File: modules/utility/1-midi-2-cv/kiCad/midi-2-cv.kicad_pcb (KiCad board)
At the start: 2 copper layers, 101 x 110 mm, 174 parts, among them J1 Conn_01x03, J3 SD-50BV (DIN5), J4 Conn_01x03, J5 BOOT_RUN, J6 Conn_01x04, Q1 BC848, Q2 BC848, Q3 BC848, Q4 BC848, SW1 ON-OFF-ON, U1 6N135, U10 MCP4728, U11 STM32F411RETx, U2 L78L05_SOT89, U3 MCP4728, U4 TL074, U5 MCP4728, U6 TL074, U7 AMS1117-3.3, U8 TL074, U9 TL074, Y2 20MHZ

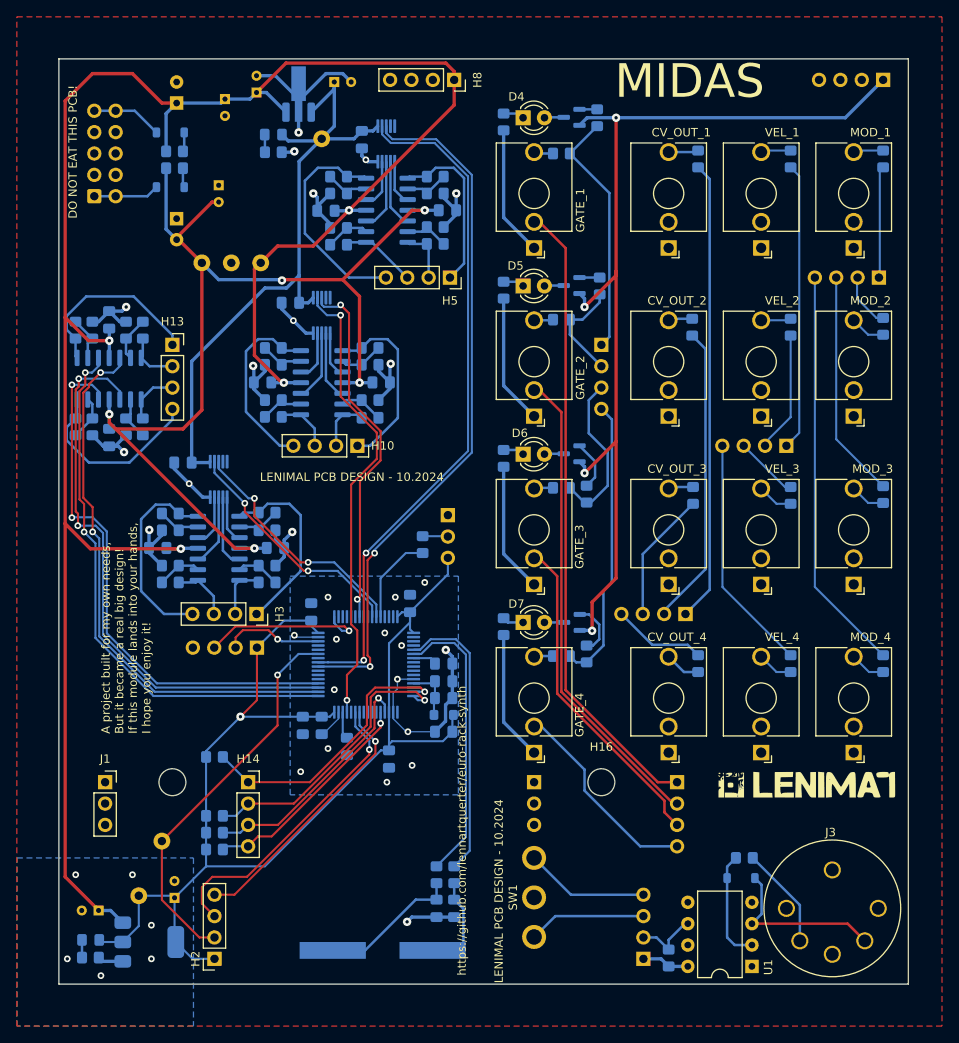
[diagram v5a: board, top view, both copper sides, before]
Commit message: debugging and rework for ricochet, midas, wolkje. Added IBOM for drums and other modules.
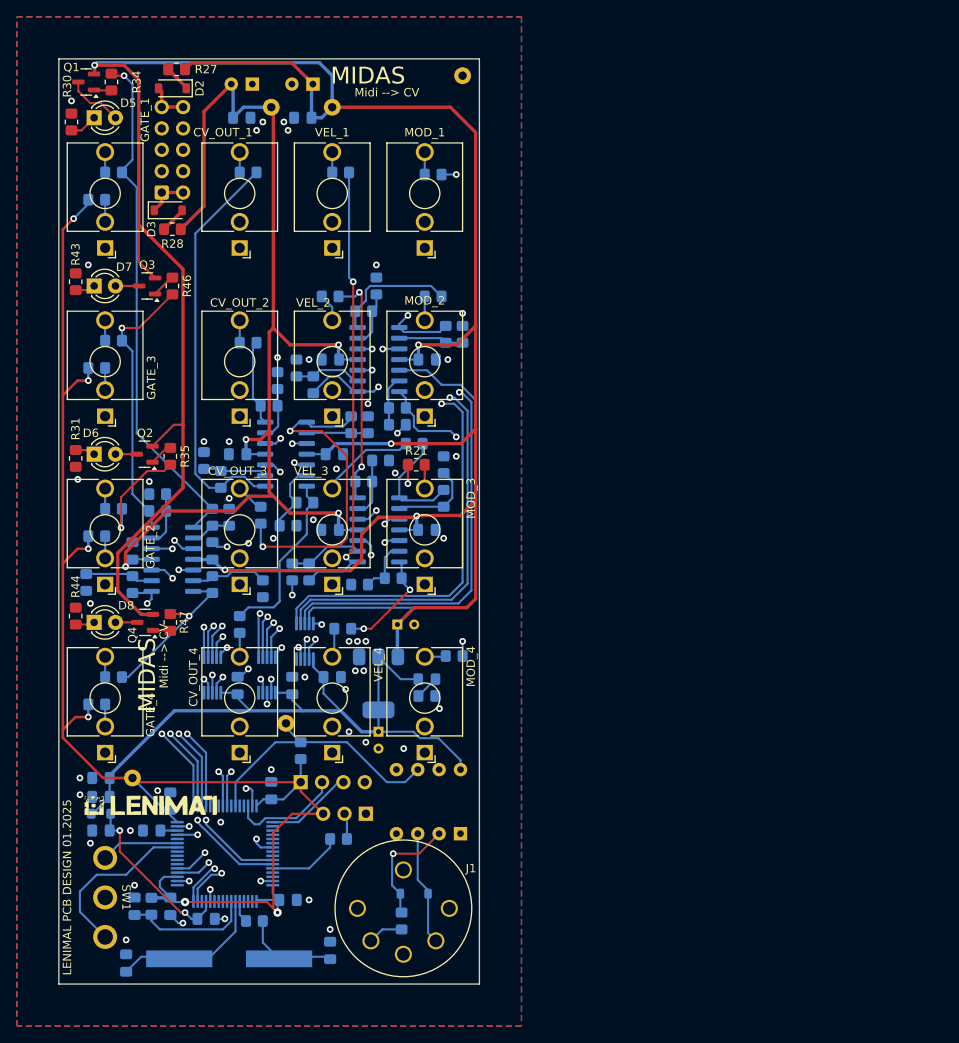
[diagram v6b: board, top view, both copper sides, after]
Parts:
- removed C30, C31, C32, C34: 100nF, Capacitor_SMD:C_0805_2012Metric_Pad1.18x1.45mm_HandSolder
- removed C33: 10uF, Capacitor_SMD:C_0805_2012Metric_Pad1.18x1.45mm_HandSolder
- removed C35: 10nF, Capacitor_SMD:C_0805_2012Metric_Pad1.18x1.45mm_HandSolder
- removed C36, C37: 1uF, Capacitor_SMD:C_0805_2012Metric_Pad1.18x1.45mm_HandSolder
- removed C38, C39: 10pF, Capacitor_SMD:C_0805_2012Metric_Pad1.18x1.45mm_HandSolder
- removed C40: 2.2uF, Capacitor_SMD:C_0805_2012Metric_Pad1.18x1.45mm_HandSolder
- removed the D8 at (75.5, 59.0)
- removed D9: LED, LED_SMD:LED_0805_2012Metric_Pad1.15x1.40mm_HandSolder
- removed the G*** at (139.0, 136.3)
- removed the G*** at (86.0, 139.5)
- removed the G*** at (139.1, 136.2)
- removed H10, H13, H14, H2, H3, H5, H8: PinSocket_01x04, Synth:PinSocket_1x04_P2.54mm_Vertical
- removed H11, H12, H15, H4, H6, H9: PinHeader_01x04, Synth:PinHeader_1x04_P2.54mm_Vertical
- removed H16, H17: MountingHole, MountingHole:MountingHole_3.2mm_M3
- removed H7: Conn_02x05_PWR_Eurorack, Synth:IDC-Header_2x05_P2.54mm_Vertical
- removed the J1 at (55.5, 136.0)
- removed J4: Conn_01x03, Connector_PinHeader_2.54mm:PinHeader_1x03_P2.54mm_Vertical
- removed J5: BOOT_RUN, Connector_PinHeader_2.54mm:PinHeader_1x03_P2.54mm_Vertical
- removed J6: Conn_01x04, Connector_PinHeader_2.54mm:PinHeader_1x04_P2.54mm_Vertical
- removed R70, R71: 2K, Resistor_SMD:R_0805_2012Metric_Pad1.20x1.40mm_HandSolder
- removed TP6: MIDI_IN, Connector_Pin:Pin_D1.0mm_L10.0mm
- removed U9: TL074, Synth:SOIC-14
- removed Y2: 20MHZ, Crystal:Crystal_SMD_HC49-SD_HandSoldering
- added C18: 100nF, Capacitor_SMD:C_0805_2012Metric_Pad1.18x1.45mm_HandSolder, B.Cu at (75.2, 137.0)
- added C19: 100nF, Capacitor_SMD:C_0805_2012Metric_Pad1.18x1.45mm_HandSolder, B.Cu at (63.2, 138.2)
- added C20: 100nF, Capacitor_SMD:C_0805_2012Metric_Pad1.18x1.45mm_HandSolder, B.Cu at (77.2, 150.0)
- added C21: 100nF, Capacitor_SMD:C_0805_2012Metric_Pad1.18x1.45mm_HandSolder, B.Cu at (63.2, 150.8)
- added C22: 10uF, Capacitor_SMD:C_0805_2012Metric_Pad1.18x1.45mm_HandSolder, B.Cu at (55.0, 135.5)
- added C23: 100nF, Capacitor_SMD:C_0805_2012Metric_Pad1.18x1.45mm_HandSolder, B.Cu at (59.0, 150.8)
- added C24: 100nF, Capacitor_SMD:C_0805_2012Metric_Pad1.18x1.45mm_HandSolder, B.Cu at (67.5, 152.2)
- added C25: 1uF, Capacitor_SMD:C_0805_2012Metric_Pad1.18x1.45mm_HandSolder, B.Cu at (55.0, 141.8)
- added C26: 1uF, Capacitor_SMD:C_0805_2012Metric_Pad1.18x1.45mm_HandSolder, B.Cu at (55.0, 137.8)
- added D4: LED, LED_SMD:LED_0805_2012Metric_Pad1.15x1.40mm_HandSolder, B.Cu at (93.8, 123.8)
- added G***: LOGO, Synth:lenimal_logo_full, F.Cu at (61.0, 138.8)
- added G***: LOGO, Synth:lenimal_logo_full, B.Cu at (61.2, 85.5)
- added J2: BOOT_RUN, Connector_PinHeader_2.54mm:PinHeader_1x03_P2.54mm_Vertical, B.Cu at (86.5, 139.8)
- added J3: Conn_01x04, Connector_PinHeader_2.54mm:PinHeader_1x04_P2.54mm_Vertical, B.Cu at (78.8, 136.0)
- added R68: 10R, Resistor_SMD:R_0805_2012Metric_Pad1.20x1.40mm_HandSolder, B.Cu at (73.2, 152.5)
- added Y1: 20MHZ, Crystal:Crystal_SMD_HC49-SD_HandSoldering, B.Cu at (70.2, 157.0)
- C15, C16: value 0.1uF -> 10uF; footprint Capacitor_SMD:C_0805_2012Metric_Pad1.18x1.45mm_HandSolder -> Capacitor_THT:CP_Radial_D4.0mm_P2.00mm
- C27, C28: value 10uF -> 10pF; footprint Capacitor_THT:CP_Radial_D4.0mm_P2.00mm -> Capacitor_SMD:C_0805_2012Metric_Pad1.18x1.45mm_HandSolder
- C29: value 100nF -> 2.2uF
- C3: value 10uF -> 47uF; footprint Capacitor_THT:CP_Radial_D4.0mm_P2.00mm -> Capacitor_THT:CP_Radial_D5.0mm_P2.50mm
- C4: value 47uF -> 0.1uF; footprint Capacitor_THT:CP_Radial_D6.3mm_P2.50mm -> Capacitor_SMD:C_0805_2012Metric_Pad1.18x1.45mm_HandSolder
- C5: footprint Capacitor_THT:CP_Radial_D6.3mm_P2.50mm -> Capacitor_THT:CP_Radial_D5.0mm_P2.50mm
- C6: value 10uF -> 0.1uF; footprint Capacitor_THT:CP_Radial_D4.0mm_P2.00mm -> Capacitor_SMD:C_0805_2012Metric_Pad1.18x1.45mm_HandSolder
- C7, C8: footprint Capacitor_THT:CP_Radial_D4.0mm_P2.00mm -> Capacitor_SMD:C_0805_2012Metric_Pad1.18x1.45mm_HandSolder
- D2, D3, Q1, Q2, Q3, Q4, R27, R28, R47: moved to F.Cu
- H1: value PinHeader_01x04 -> Conn_02x05_PWR_Eurorack; footprint Synth:PinHeader_1x04_P2.54mm_Vertical -> Synth:IDC-Header_2x05_P2.54mm_Vertical
- R10, R19, R22, R7: value 30K [0.1%] -> 10K [0.1%]
- R11, R14, R23, R26, R62: value 1K -> 30K [0.1%]
- R13, R25, R61: value 1K -> 10K [0.1%]
- R15, R18, R3, R6: value 10K [0.1%] -> 1K
- R17, R5: value 10K [0.1%] -> 30K [0.1%]
- R21: value 30K [0.1%] -> 1K; moved to F.Cu
- R29: value 10K [0.1%] -> 2K
- R30, R31: value 10K [0.1%] -> 470R; moved to F.Cu
- R32: value 10K [0.1%] -> 100K
- R33: value 30K [0.1%] -> 100K
- R34, R35: value 30K [0.1%] -> 22K; moved to F.Cu
- R36, R9: value 30K [0.1%] -> 1K
- R38, R40, R50: value 1K -> 68K
- R39: value 1K -> 100K
- R41, R42, R53: value 68K -> 100K
- R43, R44: value 100K -> 470R; moved to F.Cu
- R45: value 470R -> 100K
- R46: value 470R -> 22K; moved to F.Cu
- R48, R60: value 22K -> 1K
- R52: value 100K -> 68K
- R54: value 68K -> 1K
- R55, R64: value 100K -> 10K [0.1%]
- R56: value 100K -> 30K [0.1%]
- R57: value 470R -> 1K
- R58: value 470R -> 10K [0.1%]
- R59: value 22K -> 30K [0.1%]
- R63: value 100K -> 1K
- R65: value 10K -> 30K [0.1%]
- R66, R67: value 10R -> 10K
- TP1: value GND -> MIDI_IN
- TP2: value +12V -> +3.3V
- TP3: value -12V -> +12V
- TP4: value +5V -> GND
- TP5: value +3.3V -> -12V
- U1: value 6N135 -> 6N135-L; moved to B.Cu
- U2: value L78L05_SOT89 -> TL074; footprint Package_TO_SOT_SMD:SOT-89-3_Handsoldering -> Synth:SOIC-14
- U7: value AMS1117-3.3 -> TL074; footprint Package_TO_SOT_SMD:SOT-223-3_TabPin2 -> Synth:SOIC-14
- U8: value TL074 -> AMS1117-3.3; footprint Synth:SOIC-14 -> Package_TO_SOT_SMD:SOT-223-3_TabPin2
- moved H1 107.6 mm to (62.2, 65.9)
- moved R40 97.7 mm to (53.2, 112.2)
- moved TP5 95.1 mm to (75.2, 55.8)
- moved R45 84.5 mm to (54.5, 126.8), turned to 180 degrees
- moved R37 83.3 mm to (56.5, 103.5), turned to 180 degrees
- moved R49 81.9 mm to (56.5, 123.5)
- moved R47 78.6 mm to (63.2, 117.0), turned to -90 degrees
- moved R39 70.9 mm to (68.2, 104.5), turned to 90 degrees
- moved R38 66.8 mm to (70.2, 104.5)
- moved R26 64.9 mm to (90.2, 91.5), turned to 0 degrees
- moved R25 64.4 mm to (90.2, 93.5), turned to 180 degrees
- moved C2 64.0 mm to (82.5, 123.5), turned to 180 degrees
- moved TP2 63.1 mm to (58.8, 135.5)
- moved R14 62.1 mm to (79.2, 102.8), turned to 0 degrees
- moved U5 59.9 mm to (79.2, 119.2), turned to 90 degrees
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- renumbered D4 to D5, D5 to D7, D7 to D8, GATE_3 to GATE_2, GATE_2 to GATE_3, J3 to J1
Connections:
- C1 pad 2: +5V -> +3.3V
- C10 pad 1: GNDREF -> +12V
- C10 pad 2: -12V -> GNDREF
- C11 pad 1: +12V -> GNDREF
- C11 pad 2: GNDREF -> -12V
- C13 pad 1: +12V -> GNDREF
- C13 pad 2: GNDREF -> -12V
- C16 pad 1: GNDREF -> +3.3V
- C16 pad 2: -12V -> GNDREF
- C17 pad 2: +5V -> +3.3V
- C2 pad 2: +5V -> +3.3V
- C27 pad 1: +12V -> Net-(C27-Pad1)
- C28 pad 1: +3.3V -> /STM32F411RE/HSC_OUT
- C29 pad 1: GNDREF -> /STM32F411RE/VCap
- C29 pad 2: +3.3V -> GNDREF
- C6 pad 1: +5V -> GNDREF
- C6 pad 2: GNDREF -> -12V
- C8 pad 1: GNDREF -> +12V
- C8 pad 2: -12V -> GNDREF
- D5 pad 1: Net-(D4-K) -> Net-(D5-K)
- D7 pad 1: Net-(D5-K) -> Net-(D7-K)
- D7 pad 2: Net-(D5-A) (its old number) -> Net-(D7-A)
- D8 pad 1: Net-(D7-K) -> Net-(D8-K)
- GATE_1 pad TN: Net-(H15A-Pin_1) -> /STM32F411RE/GATE_1_IN
- GATE_2 pad T: Net-(GATE_3-PadT) -> Net-(GATE_2-PadT)
- GATE_2 pad TN: Net-(H15C-Pin_3) -> /STM32F411RE/GATE_3_IN
- GATE_3 pad T: Net-(GATE_2-PadT) -> Net-(GATE_3-PadT)
- GATE_3 pad TN: Net-(H15B-Pin_2) -> /STM32F411RE/GATE_2_IN
- GATE_4 pad TN: Net-(H15D-Pin_4) -> /STM32F411RE/GATE_4_IN
- H1 pad 1: +3.3V -> Net-(D3-K)
- H1 pad 2: Net-(H1B-Pin_2) -> Net-(D3-K)
- H1 pad 3: Net-(H1C-Pin_3) -> GNDREF
- H1 pad 4: Net-(H1D-Pin_4) -> GNDREF
- Q2 pad 3: Net-(D5-A) (its old number) -> Net-(D6-A)
- Q3 pad 3: Net-(D6-A) -> Net-(D7-A)
- R10 pad 1: Net-(U4B--) -> GNDREF
- R10 pad 2: Net-(H3D-Pin_4) -> Net-(U2A--)
- R11 pad 1: Net-(H4B-Pin_2) -> Net-(U2A--)
- R11 pad 2: Net-(CV_OUT_2-PadT) -> Net-(R11-Pad2)
- R12 pad 1: Net-(H4C-Pin_3) -> Net-(R12-Pad1)
- R12 pad 2: Net-(CV_OUT_3-PadT) -> Net-(CV_OUT_4-PadT)
- R13 pad 1: Net-(H4D-Pin_4) -> GNDREF
- R13 pad 2: Net-(CV_OUT_4-PadT) -> Net-(U2B--)
- R14 pad 1: Net-(H4A-Pin_1) -> Net-(U2B--)
- R14 pad 2: Net-(CV_OUT_1-PadT) -> Net-(R12-Pad1)
- R15 pad 1: GNDREF -> Net-(R15-Pad1)
- R15 pad 2: Net-(U6C--) -> Net-(MOD_1-PadT)
- R16 pad 2: Net-(U6D--) -> Net-(U4C--)
- R17 pad 1: GNDREF -> Net-(U4C--)
- R17 pad 2: Net-(U6A--) -> Net-(R15-Pad1)
- R18 pad 1: GNDREF -> Net-(R18-Pad1)
- R18 pad 2: Net-(U6B--) -> Net-(MOD_2-PadT)
- R19 pad 1: Net-(U6C--) -> GNDREF
- R19 pad 2: Net-(H5A-Pin_1) -> Net-(U4D--)
- R2 pad 1: Net-(H1B-Pin_2) -> /STM32F411RE/MIDI_IN
- R20 pad 1: Net-(U6D--) -> Net-(U4D--)
- R20 pad 2: Net-(H5B-Pin_2) -> Net-(R18-Pad1)
- R21 pad 1: Net-(U6A--) -> Net-(R21-Pad1)
- R21 pad 2: Net-(H5C-Pin_3) -> Net-(MOD_3-PadT)
- R22 pad 1: Net-(U6B--) -> GNDREF
- R22 pad 2: Net-(H5D-Pin_4) -> Net-(U4A--)
- R23 pad 1: Net-(H6B-Pin_2) -> Net-(U4A--)
- R23 pad 2: Net-(MOD_2-PadT) -> Net-(R21-Pad1)
- R24 pad 1: Net-(H6C-Pin_3) -> Net-(R24-Pad1)
- R24 pad 2: Net-(MOD_3-PadT) -> Net-(MOD_4-PadT)
- R25 pad 1: Net-(H6D-Pin_4) -> GNDREF
- R25 pad 2: Net-(MOD_4-PadT) -> Net-(U4B--)
- R26 pad 1: Net-(H6A-Pin_1) -> Net-(U4B--)
- R26 pad 2: Net-(MOD_1-PadT) -> Net-(R24-Pad1)
- R29 pad 2: Net-(U8C--) -> Net-(D4-K)
- R3 pad 1: GNDREF -> Net-(R3-Pad1)
- R3 pad 2: Net-(U4C--) -> Net-(CV_OUT_1-PadT)
- R30 pad 2: Net-(U8D--) -> Net-(D5-K)
- R31 pad 2: Net-(U8A--) -> Net-(D6-K)
- R32 pad 1: GNDREF -> /STM32F411RE/GATE_1_IN
- R32 pad 2: Net-(U8B--) -> +3.3V
- R33 pad 1: Net-(U8C--) -> /STM32F411RE/GATE_3_IN
- R33 pad 2: Net-(H10A-Pin_1) -> +3.3V
- R34 pad 1: Net-(U8D--) -> Net-(Q1-B)
- R34 pad 2: Net-(H10B-Pin_2) -> Net-(R34-Pad2)
- R35 pad 1: Net-(U8A--) -> Net-(R35-Pad1)
- R35 pad 2: Net-(H10C-Pin_3) -> Net-(Q2-B)
- R36 pad 1: Net-(U8B--) -> Net-(R34-Pad2)
- R36 pad 2: Net-(H10D-Pin_4) -> Net-(GATE_1-PadT)
- R37 pad 1: Net-(H11B-Pin_2) -> Net-(R35-Pad1)
- R37 pad 2: Net-(R37-Pad2) -> Net-(GATE_2-PadT)
- R38 pad 1: Net-(H11C-Pin_3) -> GNDREF
- R38 pad 2: Net-(R38-Pad2) -> Net-(U7A--)
- R39 pad 1: Net-(H11D-Pin_4) -> Net-(U7A--)
- R39 pad 2: Net-(R39-Pad2) -> Net-(R34-Pad2)
- R4 pad 2: Net-(U4D--) -> Net-(U2C--)
- R40 pad 1: Net-(H11A-Pin_1) -> GNDREF
- R40 pad 2: Net-(R40-Pad2) -> Net-(U7C--)
- R41 pad 1: GNDREF -> Net-(U7C--)
- R41 pad 2: Net-(U9A--) -> Net-(R35-Pad1)
- R42 pad 1: GNDREF -> /STM32F411RE/GATE_2_IN
- R42 pad 2: Net-(U9B--) -> +3.3V
- R43 pad 1: Net-(U9A--) -> GNDREF
- R43 pad 2: Net-(H13A-Pin_1) -> Net-(D7-K)
- R44 pad 1: Net-(U9B--) -> GNDREF
- R44 pad 2: Net-(H13B-Pin_2) -> Net-(D8-K)
- R45 pad 1: GNDREF -> /STM32F411RE/GATE_4_IN
- R45 pad 2: Net-(D4-K) -> +3.3V
- R46 pad 1: GNDREF -> Net-(R46-Pad1)
- R46 pad 2: Net-(D5-K) -> Net-(Q3-B)
- R47 pad 1: Net-(H12A-Pin_1) -> Net-(R47-Pad1)
- R47 pad 2: Net-(Q1-B) -> Net-(Q4-B)
- R48 pad 1: Net-(H12B-Pin_2) -> Net-(R46-Pad1)
- R48 pad 2: Net-(Q2-B) -> Net-(GATE_3-PadT)
- R49 pad 1: Net-(H12A-Pin_1) -> Net-(R47-Pad1)
- R49 pad 2: Net-(GATE_1-PadT) -> Net-(GATE_4-PadT)
- R5 pad 1: GNDREF -> Net-(U2C--)
- R5 pad 2: Net-(U4A--) -> Net-(R3-Pad1)
- R50 pad 1: Net-(H12B-Pin_2) -> GNDREF
- R50 pad 2: Net-(GATE_2-PadT) -> Net-(U7D--)
- R51 pad 1: /STM32F411RE/GATE_1_IN -> Net-(U7D--)
- R51 pad 2: +3.3V -> Net-(R46-Pad1)
- R52 pad 1: /STM32F411RE/GATE_2_IN -> GNDREF
- R52 pad 2: +3.3V -> Net-(U7B--)
- R53 pad 1: GNDREF -> Net-(U7B--)
- R53 pad 2: Net-(U9C--) -> Net-(R47-Pad1)
- R54 pad 1: GNDREF -> Net-(R54-Pad1)
- R54 pad 2: Net-(U9D--) -> Net-(R54-Pad2)
- R55 pad 1: Net-(U9C--) -> GNDREF
- R55 pad 2: Net-(H13C-Pin_3) -> Net-(U6C--)
- R56 pad 1: Net-(U9D--) -> Net-(U6C--)
- R56 pad 2: Net-(H13D-Pin_4) -> Net-(R54-Pad1)
- R57 pad 1: GNDREF -> Net-(R57-Pad1)
- R57 pad 2: Net-(D6-K) -> Net-(R57-Pad2)
- R58 pad 2: Net-(D7-K) -> Net-(U6D--)
- R59 pad 1: Net-(H12C-Pin_3) -> Net-(U6D--)
- R59 pad 2: Net-(Q3-B) -> Net-(R57-Pad1)
- R6 pad 1: GNDREF -> Net-(R6-Pad1)
- R6 pad 2: Net-(U4B--) -> Net-(CV_OUT_2-PadT)
- R60 pad 1: Net-(H12D-Pin_4) -> Net-(R60-Pad1)
- R60 pad 2: Net-(Q4-B) -> Net-(R60-Pad2)
- R61 pad 1: Net-(H12C-Pin_3) -> GNDREF
- R61 pad 2: Net-(GATE_3-PadT) -> Net-(U6A--)
- R62 pad 1: Net-(H12D-Pin_4) -> Net-(U6A--)
- R62 pad 2: Net-(GATE_4-PadT) -> Net-(R60-Pad1)
- R63 pad 1: /STM32F411RE/GATE_3_IN -> Net-(R63-Pad1)
- R63 pad 2: +3.3V -> Net-(R63-Pad2)
- R64 pad 1: /STM32F411RE/GATE_4_IN -> GNDREF
- R64 pad 2: +3.3V -> Net-(U6B--)
- R65 pad 1: /STM32F411RE/BOOT0 -> Net-(U6B--)
- R65 pad 2: /STM32F411RE/BOOT0_MCU -> Net-(R63-Pad1)
- R66 pad 1: Net-(C38-Pad1) -> /STM32F411RE/NRST
- R66 pad 2: /STM32F411RE/HSC_IN -> +3.3V
- R67 pad 1: Net-(C39-Pad1) -> /STM32F411RE/BOOT0
- R67 pad 2: /STM32F411RE/HSC_OUT -> /STM32F411RE/BOOT0_MCU
- R7 pad 1: Net-(U4C--) -> GNDREF
- R7 pad 2: Net-(H3A-Pin_1) -> Net-(U2D--)
- R8 pad 1: Net-(U4D--) -> Net-(U2D--)
- R8 pad 2: Net-(H3B-Pin_2) -> Net-(R6-Pad1)
- R9 pad 1: Net-(U4A--) -> Net-(R11-Pad2)
- R9 pad 2: Net-(H3C-Pin_3) -> Net-(CV_OUT_3-PadT)
- SW1 pad 1: Net-(H1C-Pin_3) -> /STM32F411RE/MODE_SW_1
- SW1 pad 3: Net-(H1D-Pin_4) -> /STM32F411RE/MODE_SW_2
- TP1 pad 1: GNDREF -> /STM32F411RE/MIDI_IN
- TP2 pad 1: +12V -> +3.3V
- TP3 pad 1: -12V -> +12V
- TP4 pad 1: +5V -> GNDREF
- TP5 pad 1: +3.3V -> -12V
- U1 pad 6: Net-(H1B-Pin_2) -> /STM32F411RE/MIDI_IN
- U10 pad 1: +5V -> +3.3V
- U10 pad 4: unconnected-(U10-~{LDAC}-Pad4) -> GNDREF
- U2 pad 1: +5V -> Net-(R11-Pad2)
- U2 pad 2: GNDREF -> Net-(U2A--)
- U2 pad 3: +12V -> Net-(U2A-+)
- U3 pad 1: +5V -> +3.3V
- U3 pad 4: unconnected-(U3-~{LDAC}-Pad4) -> GNDREF
- U3 pad 6: Net-(U3-VOUTA) -> Net-(U2C-+)
- U3 pad 7: Net-(U3-VOUTB) -> Net-(U2D-+)
- U3 pad 8: Net-(U3-VOUTC) -> Net-(U2A-+)
- U3 pad 9: Net-(U3-VOUTD) -> Net-(U2B-+)
- U4 pad 1: Net-(H3C-Pin_3) -> Net-(R21-Pad1)
- U4 pad 10: Net-(U3-VOUTA) -> Net-(U4C-+)
- U4 pad 12: Net-(U3-VOUTB) -> Net-(U4D-+)
- U4 pad 14: Net-(H3B-Pin_2) -> Net-(R18-Pad1)
- U4 pad 3: Net-(U3-VOUTC) -> Net-(U4A-+)
- U4 pad 5: Net-(U3-VOUTD) -> Net-(U4B-+)
- U4 pad 7: Net-(H3D-Pin_4) -> Net-(R24-Pad1)
- U4 pad 8: Net-(H3A-Pin_1) -> Net-(R15-Pad1)
- U5 pad 1: +5V -> +3.3V
- U5 pad 4: unconnected-(U5-~{LDAC}-Pad4) -> GNDREF
- U5 pad 6: Net-(U5-VOUTA) -> Net-(U4C-+)
- U5 pad 7: Net-(U5-VOUTB) -> Net-(U4D-+)
- U5 pad 8: Net-(U5-VOUTC) -> Net-(U4A-+)
- U5 pad 9: Net-(U5-VOUTD) -> Net-(U4B-+)
- U6 pad 1: Net-(H5C-Pin_3) -> Net-(R60-Pad1)
- U6 pad 10: Net-(U5-VOUTA) -> Net-(U10-VOUTA)
- U6 pad 12: Net-(U5-VOUTB) -> Net-(U10-VOUTB)
- U6 pad 14: Net-(H5B-Pin_2) -> Net-(R57-Pad1)
- U6 pad 3: Net-(U5-VOUTC) -> Net-(U10-VOUTC)
- U6 pad 5: Net-(U5-VOUTD) -> Net-(U10-VOUTD)
- U6 pad 7: Net-(H5D-Pin_4) -> Net-(R63-Pad1)
- U6 pad 8: Net-(H5A-Pin_1) -> Net-(R54-Pad1)
- U7 pad 1: GNDREF -> Net-(R34-Pad2)
- U7 pad 2: +3.3V -> Net-(U7A--)
- U7 pad 3: +12V -> /STM32F411RE/GATE_1_OUT
- U8 pad 1: Net-(H10C-Pin_3) -> GNDREF
- U8 pad 2: Net-(U8A--) -> +3.3V
- U8 pad 3: Net-(U10-VOUTC) -> +12V
- VEL_1 pad T: Net-(R40-Pad2) -> Net-(R54-Pad2)
- VEL_2 pad T: Net-(R37-Pad2) -> Net-(R57-Pad2)
- VEL_3 pad T: Net-(R38-Pad2) -> Net-(R60-Pad2)
- VEL_4 pad T: Net-(R39-Pad2) -> Net-(R63-Pad2)
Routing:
- net GNDREF: track 195.7 -> 27.3 mm, vias 35 -> 64
- net +3.3V: track 155.6 -> 264.2 mm, vias 1 -> 6
- net +5V: track 78.3 -> 0.00 mm
- net Net-(H15A-Pin_1): track 75.4 -> 0.00 mm
- net /STM32F411RE/GATE_1_IN: track 33.5 -> 101.5 mm
- net Net-(R34-Pad2): track 0.00 -> 61.7 mm, vias 0 -> 1
- net Net-(U4D-+): track 0.00 -> 59.9 mm, vias 0 -> 2
- net Net-(U4A-+): track 0.00 -> 59.9 mm, vias 0 -> 2
- net Net-(U4C-+): track 0.00 -> 58.6 mm, vias 0 -> 2
- net Net-(H15B-Pin_2): track 56.8 -> 0.00 mm
- net Net-(U4B-+): track 0.00 -> 56.0 mm
- net +12V: track 367.0 -> 311.3 mm, vias 8 -> 5
- net Net-(H4A-Pin_1): track 54.9 -> 0.00 mm
- net Net-(R54-Pad1): track 0.00 -> 54.6 mm, vias 0 -> 2
- net /STM32F411RE/MOD_SDA: track 83.0 -> 29.6 mm
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- added copper zone on In1.Cu, net GNDREF
- added copper zone on In2.Cu, net GNDREF
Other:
- board size 101 x 110 mm -> 50 x 110 mm
- copper layers 2 -> 4
- board text added: "3.3V"
- board text added: "BOOT"
- board text added: "LENIMAL PCB DESIGN 01.2025"
- board text added: "Midi --> CV"
- board text added: "RUN"
- board text added: "STM32 F411 RETX"
- board text removed: "+3.3V"
- board text removed: "+5V"
- board text removed: "20MHZ"
- board text removed: "A project built for my own needs, But it became a real big design! If this module lands into your hands, I hope you enjoy it!"
- board text removed: "DO NOT EAT THIS PCB!"
- board text removed: "LENIMAL PCB DESIGN - 10.2024"
- board text removed: "PWR_3V"
- board text removed: "PWR_5V"
- board text removed: "STM32 F411 RET7"
- board text removed: "TL074"
- board text removed: "https://github.com/lennartquerter/euro-rack-synth"

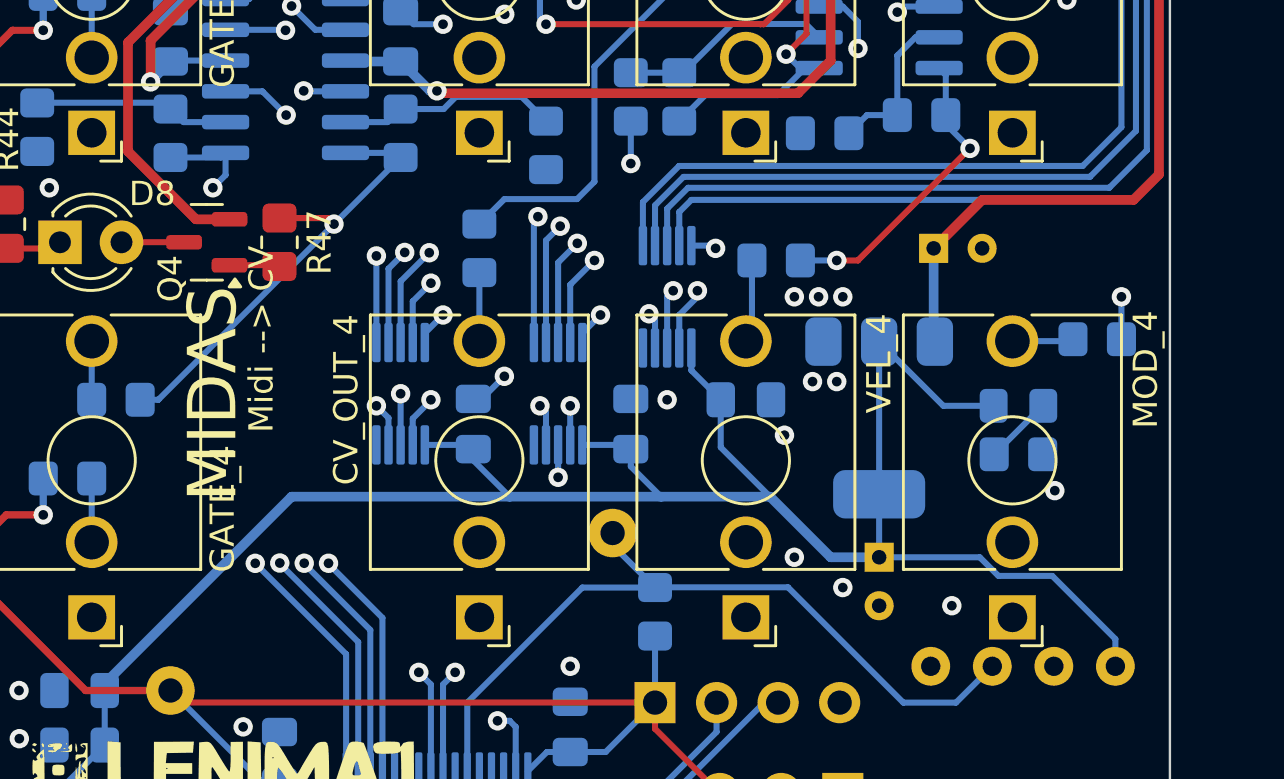
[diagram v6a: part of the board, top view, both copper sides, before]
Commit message: Preperation for Run3, wolkje, ricochet readme and final exports
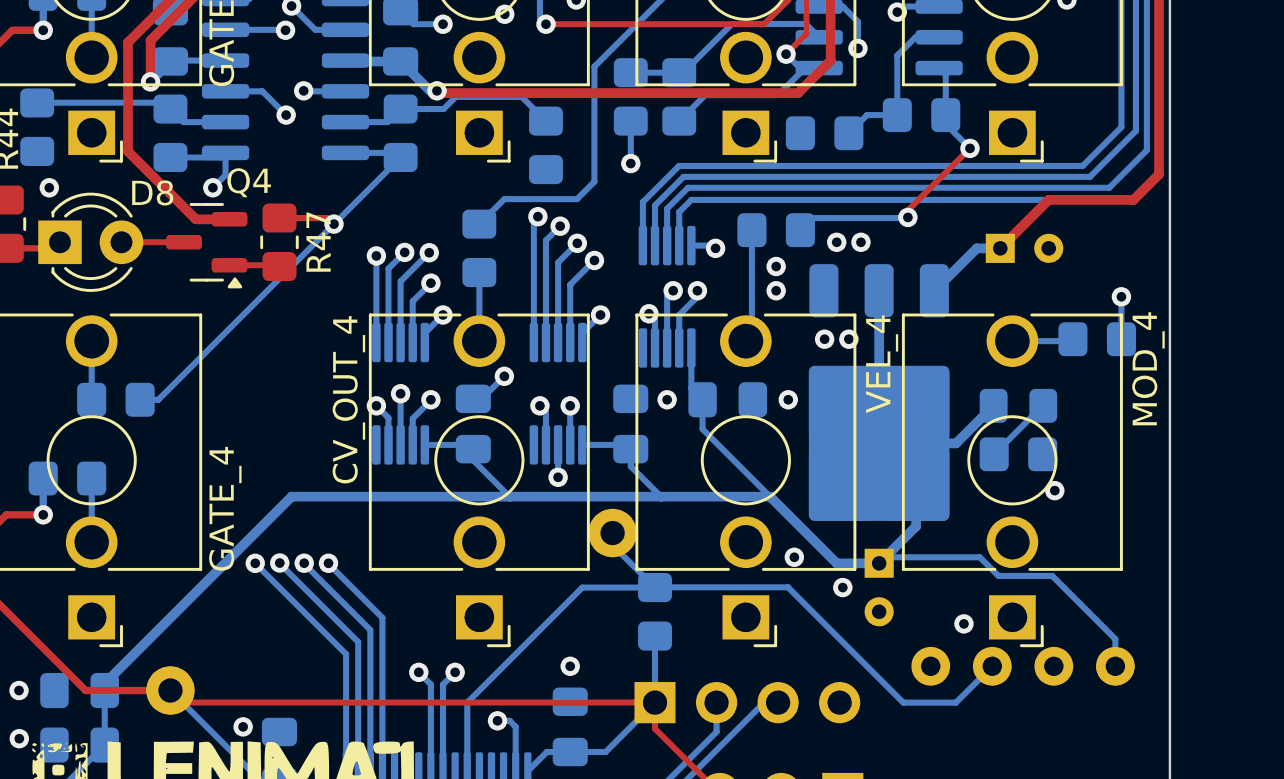
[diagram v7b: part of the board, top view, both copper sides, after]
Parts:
- U8: value AMS1117-3.3 -> LM1117DT-3.3; footprint Package_TO_SOT_SMD:SOT-223-3_TabPin2 -> Package_TO_SOT_SMD:TO-252-3_TabPin2
- moved C15 2.75 mm to (93.0, 117.2)
- moved R63 1.25 mm to (83.8, 116.5)
- moved C2 0.75 mm to (81.8, 123.5)
- moved C16 0.25 mm to (88.0, 130.2)
- moved U8 0.21 mm to (88.0, 124.0)
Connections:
- net /STM32F411RE/CV_SCL renamed /STM32F411RE/I2C_CV_SCL
- net /STM32F411RE/CV_SDA renamed /STM32F411RE/I2C_CV_SDA
- net /STM32F411RE/MIDI_IN renamed /STM32F411RE/MIDI_INPUT
- net /STM32F411RE/MOD_SCL renamed /STM32F411RE/I2C_MOD_SCL
- net /STM32F411RE/MOD_SDA renamed /STM32F411RE/I2C_MOD_SDA
- net /STM32F411RE/VEL_SCL renamed /STM32F411RE/I2C_VEL_SCL
- net /STM32F411RE/VEL_SDA renamed /STM32F411RE/I2C_VEL_SDA
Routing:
- net +12V: track 311.3 -> 308.1 mm
- net Net-(R63-Pad2): track 3.43 -> 4.68 mm
- net +3.3V: track 264.2 -> 265.3 mm
- net GNDREF: vias 64 -> 65

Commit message: updates to Midas, ready for run 3
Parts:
- moved G*** 11.7 mm to (69.0, 76.8), turned to 180 degrees
- moved TP4 1.50 mm to (96.5, 52.0), turned to 0 degrees
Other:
- board text added: "Converting MIDI signals to CV"
- board text added: "REV.2"
- board text removed: "Midi --> CV"
